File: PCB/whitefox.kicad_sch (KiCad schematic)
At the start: 58 parts, among them J1 Micro_SD_Card, J3 Conn_02x16_Odd_Even, J4 Conn_02x16_Odd_Even, J5 USB_C_Receptacle_USB2.0_16P, J6 Conn_01x02, J7 Conn_01x03_MountingPin, Q1 AO3400A, SW1 SW_Push, SW2 SW_Push, U1 W25Q128JVS, U2 RP2350B-QFN80, U4 TP4056-42-ESOP8, U5 NCP1117-3.3_SOT223, U6 NCP1117-3.3_SOT223, Y1 Crystal_GND24

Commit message: upload to github
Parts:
- removed D1, D2, D3, D4: SK6812MINI-E, LED_SMD:LED_SK6812MINI-E_3.2x2.8mm_P1.5mm_ReverseMount, symbol LED:SK6812MINI-E
- removed L1: 3.3u, symbol Device:L
- removed Q1: AO3400A, Package_TO_SOT_SMD:SOT-23, symbol Transistor_FET:AO3400A
- removed U5, U6: NCP1117-3.3_SOT223, Package_TO_SOT_SMD:SOT-223-3_TabPin2, symbol Regulator_Linear:NCP1117-3.3_SOT223
- added D1, D10, D11, D2, D3, D4, D5, D6, D9: WS2812B-2020, WS2812C-2020:LED_WS2812C-2020, symbol LED:WS2812B-2020
- added L1: 3.3u, Inductor_SMD:L_0805_2012Metric, symbol custom-symbols-device:L_Polar
- added Q1: AO3401A, Package_TO_SOT_SMD:SOT-23, symbol Transistor_FET:AO3401A
- added U3, U5: AMS1117-3.3, Package_TO_SOT_SMD:SOT-223-3_TabPin2, symbol Regulator_Linear:AMS1117-3.3
- C1: renamed from C2; footprint (none) -> Capacitor_SMD:C_0402_1005Metric
- C10: renamed from C12; footprint (none) -> Capacitor_SMD:C_0402_1005Metric
- C11: renamed from C13; footprint (none) -> Capacitor_SMD:C_0402_1005Metric
- C12: renamed from C14; footprint (none) -> Capacitor_SMD:C_0402_1005Metric
- C13: renamed from C1; footprint (none) -> Capacitor_SMD:C_0402_1005Metric
- C14: renamed from C15; footprint (none) -> Capacitor_SMD:C_0402_1005Metric
- C15: renamed from C16; footprint (none) -> Capacitor_SMD:C_0402_1005Metric
- C16: renamed from C17; footprint (none) -> Capacitor_SMD:C_0402_1005Metric
- C17: renamed from C5; value 100u -> 100n; footprint (none) -> Capacitor_SMD:C_0402_1005Metric
- C18, C19: value 15p -> 33p; footprint (none) -> Capacitor_SMD:C_0402_1005Metric
- C2: renamed from C3; footprint (none) -> Capacitor_SMD:C_0402_1005Metric
- C20: renamed from C22; footprint (none) -> Capacitor_SMD:C_0402_1005Metric
- C21: renamed from C23; footprint (none) -> Capacitor_SMD:C_0402_1005Metric
- C22: renamed from C20; footprint (none) -> Capacitor_SMD:C_0402_1005Metric
- C23: renamed from C21; footprint (none) -> Capacitor_SMD:C_0402_1005Metric
- C24, C25: footprint (none) -> Capacitor_SMD:C_0402_1005Metric
- C3: renamed from C4; footprint (none) -> Capacitor_SMD:C_0402_1005Metric
- C4: renamed from C6; footprint (none) -> Capacitor_SMD:C_0402_1005Metric
- C5: renamed from C7; footprint (none) -> Capacitor_SMD:C_0402_1005Metric
- C6: renamed from C8; footprint (none) -> Capacitor_SMD:C_0402_1005Metric
- C7: renamed from C9; footprint (none) -> Capacitor_SMD:C_0402_1005Metric
- C8: renamed from C10; footprint (none) -> Capacitor_SMD:C_0402_1005Metric
- C9: renamed from C11; footprint (none) -> Capacitor_SMD:C_0402_1005Metric
- D7: renamed from D6; footprint (none) -> LED_SMD:LED_0603_1608Metric
- J1: footprint (none) -> TF-01A:TF-01A
- J2: renamed from J3; footprint (none) -> Connector_PinHeader_2.54mm:PinHeader_2x16_P2.54mm_Vertical
- J3: renamed from J4; footprint (none) -> Connector_PinHeader_2.54mm:PinHeader_2x16_P2.54mm_Vertical
- J4: renamed from J7; footprint (none) -> Connector_PinHeader_2.54mm:PinHeader_1x03_P2.54mm_Vertical
- J5: footprint (none) -> TYPE-C-31-M-12:TYPE-C-31-M-12
- J6: footprint (none) -> Connector_JST:JST_PH_S2B-PH-K_1x02_P2.00mm_Horizontal
- R1: renamed from R5; footprint (none) -> Resistor_SMD:R_0402_1005Metric
- R10: renamed from R9; footprint (none) -> Resistor_SMD:R_0402_1005Metric
- R11: footprint (none) -> Resistor_SMD:R_0402_1005Metric
- R2: renamed from R1; footprint (none) -> Resistor_SMD:R_0402_1005Metric
- R3: renamed from R2; footprint (none) -> Resistor_SMD:R_0402_1005Metric
- R4: renamed from R6; footprint (none) -> Resistor_SMD:R_0402_1005Metric
- R5: renamed from R3; footprint (none) -> Resistor_SMD:R_0402_1005Metric
- R6: renamed from R4; footprint (none) -> Resistor_SMD:R_0402_1005Metric
- R7: renamed from R10; footprint (none) -> Resistor_SMD:R_0402_1005Metric
- R8: renamed from R7; footprint (none) -> Resistor_SMD:R_0402_1005Metric
- R9: renamed from R8; footprint (none) -> Resistor_SMD:R_0402_1005Metric
- SW1, SW2: footprint (none) -> TS-1088-TS-1088-ARXXX:TS-1088-ARXXX
- renumbered D5 to D8
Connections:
- net +1V1: now also L1.1
- net +3V3: now also J2.6 (Pin_6), U3.2 (VO), U5.2 (VO)
- net +BATT: now also Q1.3 (D)
- net GND: now also J3.5 (Pin_5), D1.2 (VSS), D10.2 (VSS), D11.2 (VSS), D2.2 (VSS), D3.2 (VSS), D4.2 (VSS), D5.2 (VSS), D6.2 (VSS), D9.2 (VSS), U3.1 (GND), U5.1 (GND); no longer J3.19 (Pin_19), J3.6 (Pin_6)
- net GPIO08: no longer J2.27 (Pin_27), U2.6 (GPIO8)
- net GPIO09: no longer J2.28 (Pin_28), U2.7 (GPIO9)
- net GPIO10: now also J2.18 (Pin_18); no longer J3.9 (Pin_9)
- net GPIO11: now also J2.17 (Pin_17); no longer J3.10 (Pin_10)
- net GPIO17: now also J2.25 (Pin_25); no longer J2.21 (Pin_21)
- net GPIO18: now also J2.28 (Pin_28); no longer J2.22 (Pin_22)
- net GPIO19: now also J2.27 (Pin_27); no longer J3.20 (Pin_20)
- net GPIO32: now also J3.22 (Pin_22); no longer J3.15 (Pin_15)
- net GPIO33: now also J3.19 (Pin_19); no longer J3.16 (Pin_16)
- net GPIO34: now also J3.20 (Pin_20); no longer J3.17 (Pin_17)
- net GPIO35: now also J3.17 (Pin_17); no longer J3.18 (Pin_18)
- net GPIO36: now also J3.18 (Pin_18); no longer J3.21 (Pin_21)
- net GPIO37: now also J3.15 (Pin_15); no longer J3.22 (Pin_22)
- net GPIO38: now also J3.16 (Pin_16); no longer J3.23 (Pin_23)
- net GPIO40: now also J3.14 (Pin_14); no longer J3.25 (Pin_25)
- net GPIO41: now also J3.13 (Pin_13); no longer J3.26 (Pin_26)
- net GPIO42: now also J3.12 (Pin_12); no longer J3.27 (Pin_27)
- net GPIO43: now also J3.11 (Pin_11); no longer J3.28 (Pin_28)
- net GPIO44: now also J3.10 (Pin_10); no longer J3.29 (Pin_29)
- net GPIO45: now also J3.9 (Pin_9); no longer J3.30 (Pin_30)
- net GPIO46: now also J3.8 (Pin_8); no longer J2.29 (Pin_29)
- net GPIO47: now also J3.7 (Pin_7); no longer J2.30 (Pin_30)
- net MOSFET_OUT: now also Q1.2 (S), U5.3 (VI)
- net NEOPIXEL: now also U2.48 (GPIO39), D1.3 (DIN); no longer U2.16 (GPIO16)
- net RUN: now also J3.27 (Pin_27); no longer J2.6 (Pin_6)
- net SPI1_CSN_SD_CS: now also U2.26 (GPIO25); no longer U2.37 (GPIO29)
- net SPI1_RX_SD_MISO: now also U2.25 (GPIO24); no longer U2.36 (GPIO28)
- net SPI1_SCK_SD_SCK: now also U2.27 (GPIO26); no longer U2.38 (GPIO30)
- net SPI1_TX_SD_MOSI: now also U2.28 (GPIO27); no longer U2.39 (GPIO31)
- net SWCLK: now also J3.29 (Pin_29); no longer J3.7 (Pin_7)
- net SWDIO: now also J3.30 (Pin_30); no longer J3.8 (Pin_8)
- net VBUS: now also J3.6 (Pin_6), D1.4 (VDD), D10.4 (VDD), D11.4 (VDD), D2.4 (VDD), D3.4 (VDD), D4.4 (VDD), D5.4 (VDD), D6.4 (VDD), D9.4 (VDD), Q1.1 (G), U3.3 (VI); no longer J3.5 (Pin_5)
- net at U2.63 (VREG_LX): now also L1.2
- net GPIO24 renamed GPIO15
- net GPIO15: now also U2.14 (GPIO15); no longer U2.25 (GPIO24)
- net GPIO25 renamed GPIO14
- net GPIO14: now also U2.13 (GPIO14); no longer U2.26 (GPIO25)
- removed net GPIO26: J2.25 (Pin_25), U2.27 (GPIO26)
- net GPIO27 renamed GPIO16
- net GPIO16: now also U2.16 (GPIO16); no longer U2.28 (GPIO27)
- net GPIO39 renamed GPIO30
- net GPIO30: now also U2.38 (GPIO30); no longer U2.48 (GPIO39)
- net I2C0_SCL renamed GPIO5
- net GPIO5: now also J2.11 (Pin_11); no longer J2.16 (Pin_16)
- net I2C0_SDA renamed GPIO4
- net GPIO4: now also J2.12 (Pin_12); no longer J2.15 (Pin_15)
- net I2C1_SCL renamed GPIO7
- net GPIO7: now also J2.13 (Pin_13); no longer J2.18 (Pin_18)
- net I2C1_SDA renamed GPIO6
- net GPIO6: now also J2.14 (Pin_14); no longer J2.17 (Pin_17)
- net SPI0_CSN renamed GPIO0
- net GPIO0: now also U2.77 (GPIO0); no longer U2.78 (GPIO1)
- net SPI0_RX renamed GPIO1
- net GPIO1: now also U2.78 (GPIO1); no longer U2.77 (GPIO0)
- net SPI0_SCK renamed GPIO2
- net GPIO2: now also J2.10 (Pin_10); no longer J2.9 (Pin_9)
- net SPI0_TX renamed GPIO3
- net GPIO3: now also J2.9 (Pin_9); no longer J2.10 (Pin_10)
- removed net UART0_CTS: J2.13 (Pin_13), U2.13 (GPIO14)
- removed net UART0_RTS: J2.14 (Pin_14), U2.14 (GPIO15)
- net UART0_RX renamed GPIO13
- net GPIO13: now also J2.21 (Pin_21); no longer J2.12 (Pin_12)
- net UART0_TX renamed GPIO12
- net GPIO12: now also J2.22 (Pin_22); no longer J2.11 (Pin_11)
- net UART1_CTS renamed GPIO22
- net GPIO22: now also J3.28 (Pin_28); no longer J3.13 (Pin_13)
- net UART1_RTS renamed GPIO23
- net GPIO23: now also J3.25 (Pin_25); no longer J3.14 (Pin_14)
- net UART1_RX renamed GPIO21
- net GPIO21: now also J2.29 (Pin_29); no longer J3.12 (Pin_12)
- net UART1_TX renamed GPIO20
- net GPIO20: now also J2.30 (Pin_30); no longer J3.11 (Pin_11)
- new net: D6.1 (DOUT), D9.3 (DIN)
- new net: D5.1 (DOUT), D6.3 (DIN)
- new net: D2.1 (DOUT), D3.3 (DIN)
- new net: D1.1 (DOUT), D2.3 (DIN)
- new net: D10.1 (DOUT), D11.3 (DIN)
- new net: D10.3 (DIN), D9.1 (DOUT)
- new net: D3.1 (DOUT), D4.3 (DIN)
- new net: D4.1 (DOUT), D5.3 (DIN)
- new net GPIO28: J3.26 (Pin_26), U2.36 (GPIO28)
- new net GPIO29: J3.23 (Pin_23), U2.37 (GPIO29)
- new net GPIO31: J3.21 (Pin_21), U2.39 (GPIO31)
- new net GPIO8: J2.16 (Pin_16), U2.6 (GPIO8)
- new net GPIO9: J2.15 (Pin_15), U2.7 (GPIO9)
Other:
- note added: "3x3 NeoPixel Grid"
- note added: "L"
- note added: "MCU HERE"
- note added: "R"
- note removed: "2x2 NeoPixel Grid"
- moved on the sheet: C1, C18, C19, C2, C3, R2, R6, Y1

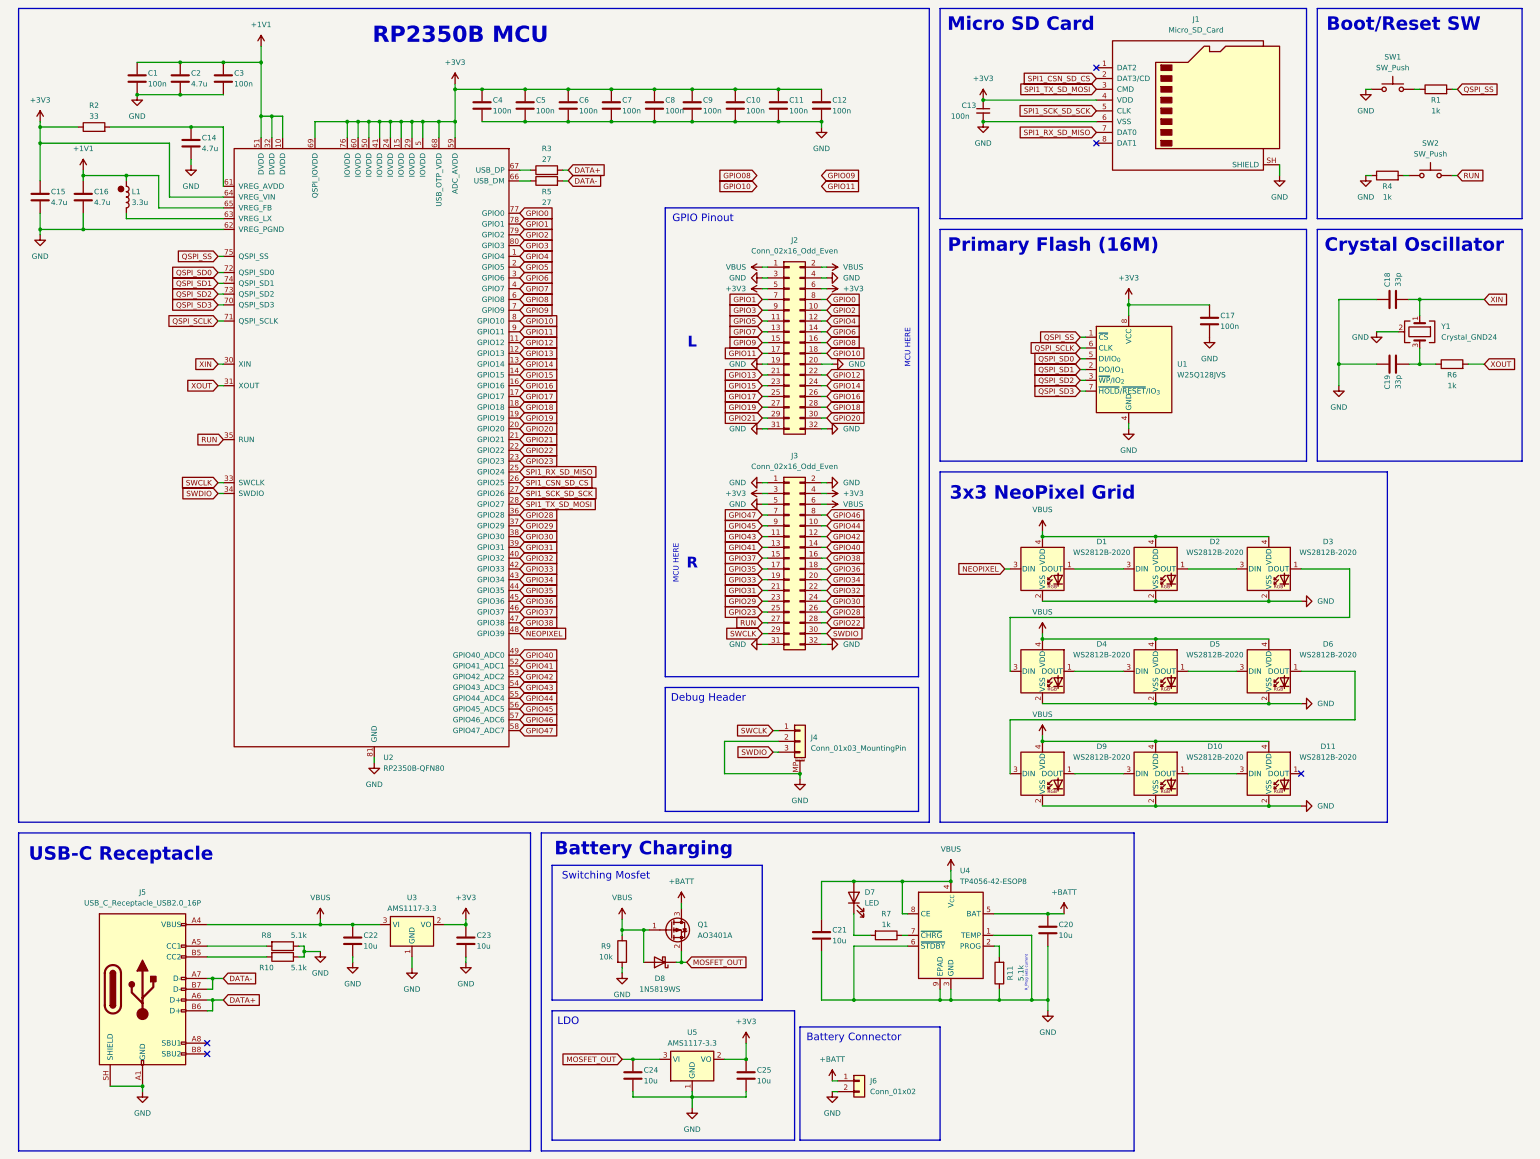
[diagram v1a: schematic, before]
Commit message: add decoupling caps
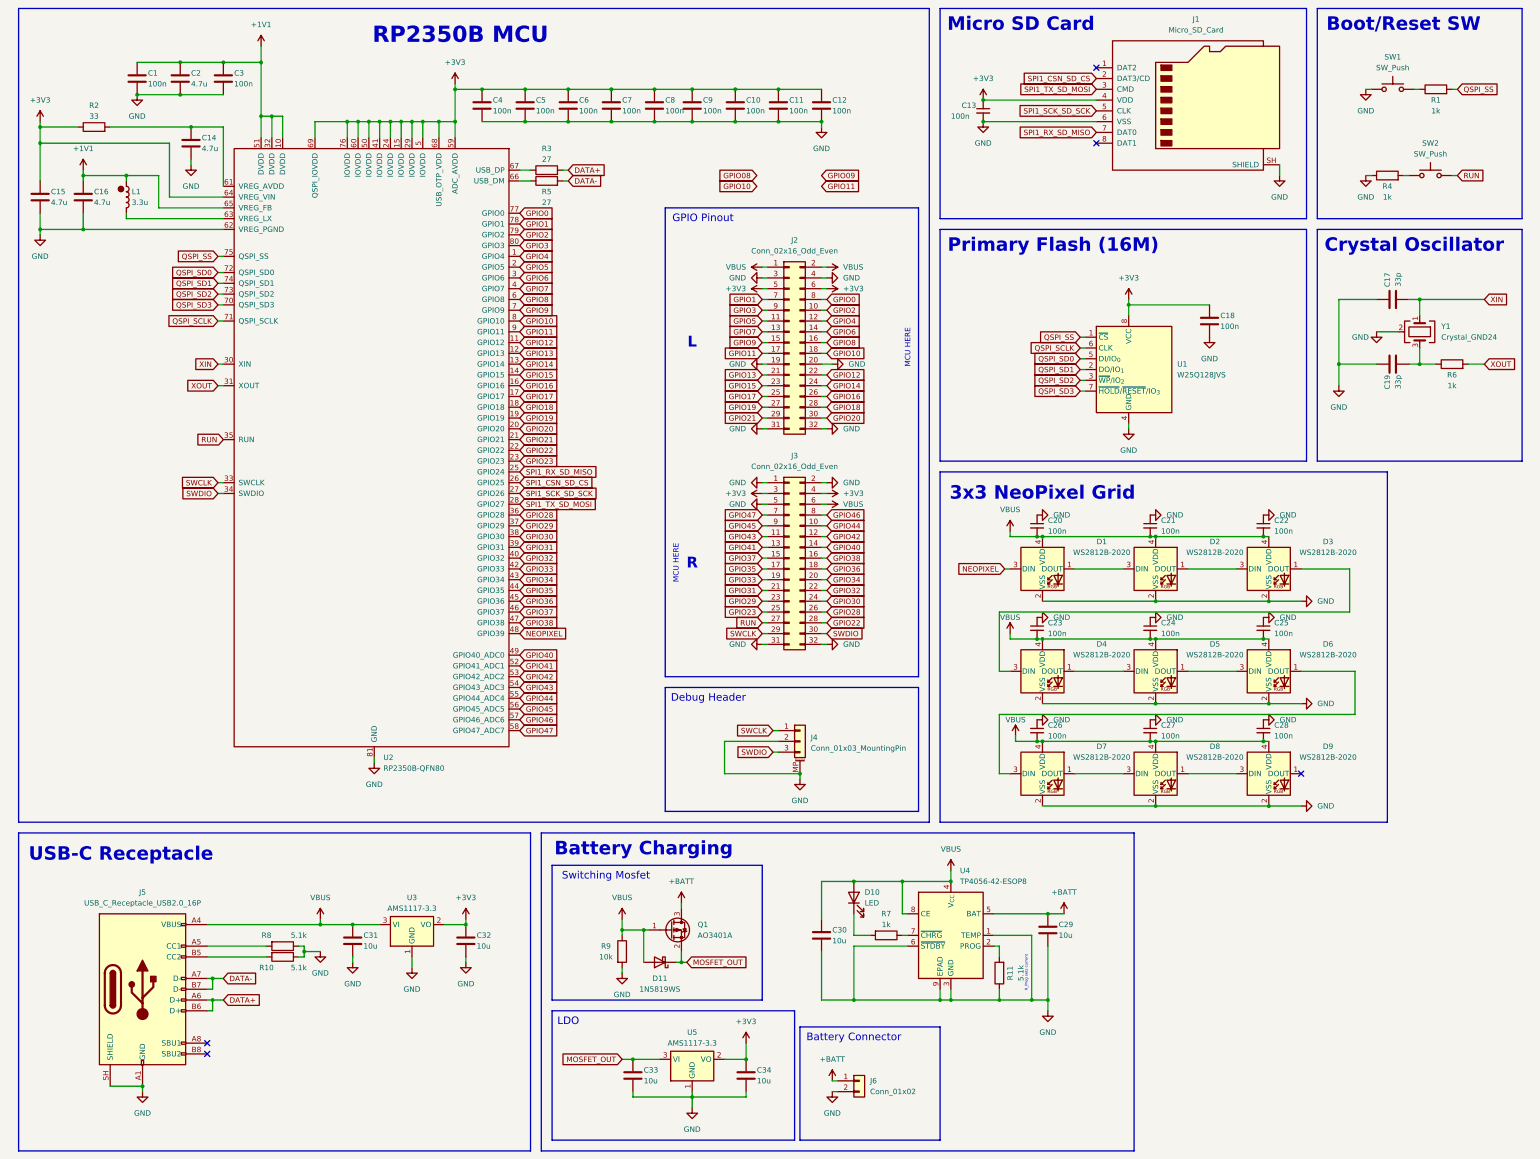
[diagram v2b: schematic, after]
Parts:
- added C20, C21, C22, C23, C24, C25, C26, C27, C28: 100n, Capacitor_SMD:C_0402_1005Metric, symbol Device:C_Small
- L1: footprint Inductor_SMD:L_0805_2012Metric -> jlc_kicad_footprint:IND-SMD_L2.0-W1.6_AOTA-B201610S3R3-101-T
- renumbered C18 to C17, C17 to C18, C20 to C29, C21 to C30, C22 to C31, C23 to C32, C24 to C33, C25 to C34, D7 to D10, D8 to D11, D9 to D7, D10 to D8, D11 to D9
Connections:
- net GND: now also C20.1, C21.1, C22.1, C23.1, C24.1, C25.1, C26.1, C27.1, C28.1
- net VBUS: now also C20.2, C21.2, C22.2, C23.2, C24.2, C25.2, C26.2, C27.2, C28.2
